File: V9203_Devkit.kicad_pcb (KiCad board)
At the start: 2 copper layers, 50 x 50 mm, 83 parts, among them J1 RJ45, J2 CONN_01X16, J3 CONN_01X12, J4 Screw_Terminal_1x04, J5 GROVE-CONNECTOR-SMD-90D(4+2P-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, J6 CONN_01X06, J7 GS3, J8 GS3, J9 CONN_01X06, U1 V9203, U2 ROF-78E, Y1 Crystal_GND24

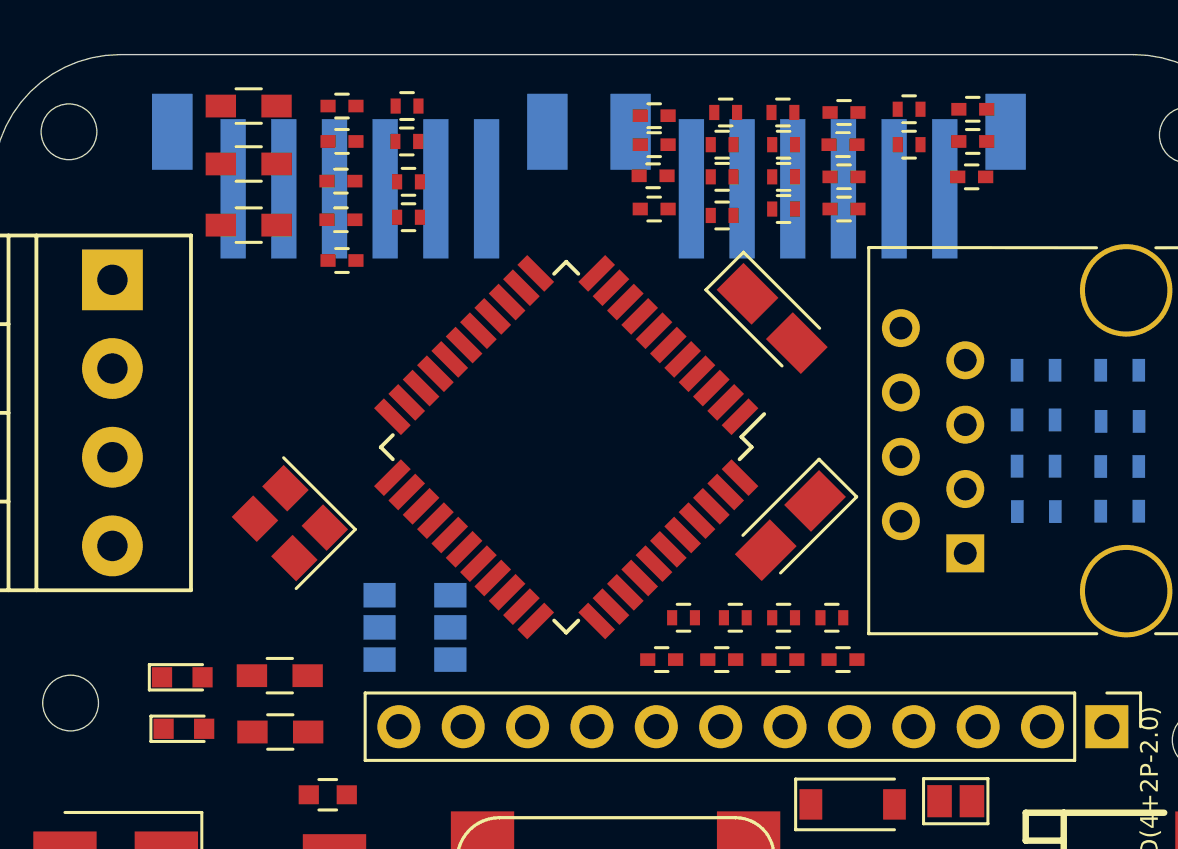
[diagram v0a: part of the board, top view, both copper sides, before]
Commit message: Added more signals to JST connector including DMA
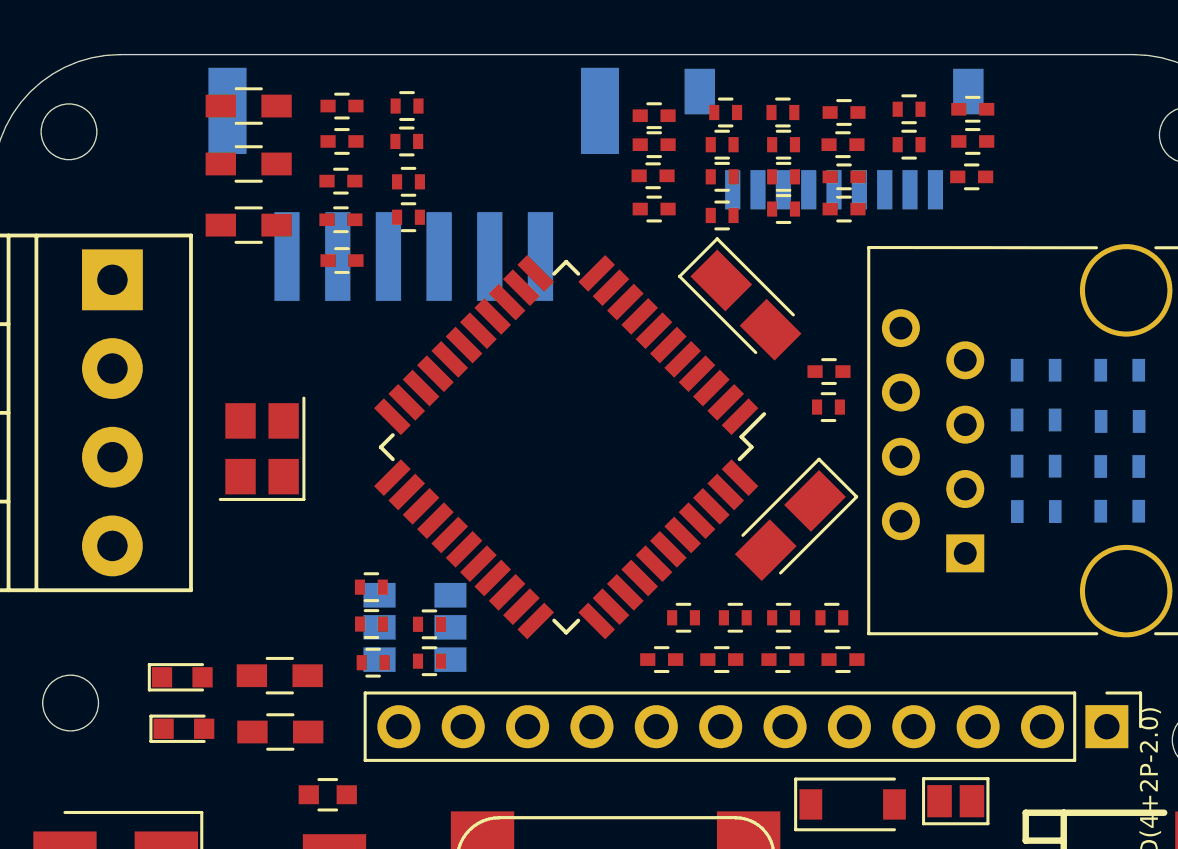
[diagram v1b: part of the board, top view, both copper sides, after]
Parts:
- added C27: C, Capacitors_SMD:C_0402, F.Cu at (143.0, 52.5)
- added R33: R, Resistors_SMD:R_0402, F.Cu at (143.0, 53.9)
- added R34: R, Resistors_SMD:R_0402, F.Cu at (124.9, 62.5)
- added R35: R, Resistors_SMD:R_0402, F.Cu at (124.9, 61.0)
- added R36: R, Resistors_SMD:R_0402, F.Cu at (127.2, 63.9)
- added R37: R, Resistors_SMD:R_0402, F.Cu at (125.0, 64.0)
- added R38: R, Resistors_SMD:R_0402, F.Cu at (127.2, 62.5)
- J6: value CONN_01X06 -> CONN_01X09; footprint Connectors_JST:JST_PH_B6B-PH-SM4-TB_06x2.00mm_Straight -> Connectors_JST:JST_SH_SM09B-SRSS-TB_09x1.00mm_Angled
- J9: footprint Connectors_JST:JST_PH_B6B-PH-SM4-TB_06x2.00mm_Straight -> Connectors_JST:JST_PH_S6B-PH-SM4-TB_06x2.00mm_Angled
- moved Y1 3.13 mm to (120.6, 55.6), turned to 90 degrees
- moved J9 2.32 mm to (126.6, 45.1), turned to 0 degrees
- moved C13 1.16 mm to (139.7, 49.9)
- moved J6 1.00 mm to (143.2, 43.4), turned to 0 degrees
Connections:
- C13 pad 2: Net-(C13-Pad2) -> +3V3
- C16 pad 1: Net-(C16-Pad1) -> +3V3
- J6 pad 6: GND -> Net-(J6-Pad6)
- U1 pad 2: Net-(C13-Pad2) -> +3V3
- U1 pad 30: Net-(J6-Pad5) -> Net-(R36-Pad1)
- U1 pad 31: Net-(J6-Pad4) -> Net-(R35-Pad1)
- U1 pad 32: Net-(J6-Pad3) -> Net-(R38-Pad1)
- U1 pad 33: Net-(J6-Pad2) -> Net-(R37-Pad1)
- U1 pad 34: Net-(J6-Pad1) -> Net-(R34-Pad1)
- U1 pad 35: Net-(U1-Pad35) -> Net-(J6-Pad3)
- U1 pad 36: Net-(U1-Pad36) -> Net-(J6-Pad2)
- U1 pad 37: Net-(U1-Pad37) -> Net-(J6-Pad1)
- U1 pad 44: Net-(C16-Pad1) -> +3V3

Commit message: Flipped connectors
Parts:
- C10, C11, C12, C15, C16, C17, C18, C19, C20, C21, C22, C5, C6, C7, C8, C9, R10, R11, R12, R13, R14, R15, R16, R2, R25, R26, R3, R4, R5, R6, R7, R8, R9: moved to B.Cu
- J6: moved to F.Cu
- J9: footprint Connectors_JST:JST_PH_S6B-PH-SM4-TB_06x2.00mm_Angled -> Connectors_JST:JST_SHL_SM06B-SHLS-TF_06x1.00mm_Angled; moved to F.Cu
- moved C22 13.4 mm to (149.4, 44.5), turned to 0 degrees
- moved C5 13.3 mm to (149.4, 43.3), turned to 180 degrees
- moved C6 13.3 mm to (149.4, 45.8), turned to 0 degrees
- moved C7 13.3 mm to (149.4, 42.2), turned to 180 degrees
- moved C10 11.8 mm to (136.8, 43.2), turned to 180 degrees
- moved C16 11.8 mm to (136.8, 41.9), turned to 180 degrees
- moved C15 11.8 mm to (136.9, 44.6), turned to 180 degrees
- moved R10 8.53 mm to (125.1, 49.0), turned to 270 degrees
- moved R2 7.95 mm to (146.7, 43.3), turned to 0 degrees
- moved R25 7.95 mm to (146.7, 44.6), turned to 0 degrees
- moved R26 7.95 mm to (146.7, 46.1), turned to 0 degrees
- moved R3 7.68 mm to (146.6, 42.0), turned to 180 degrees
- moved R16 6.84 mm to (120.7, 42.6), turned to 270 degrees
- moved R6 6.81 mm to (139.3, 41.9), turned to 180 degrees
- moved R7 6.81 mm to (139.3, 43.3), turned to 0 degrees
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
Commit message: Flipped connectors
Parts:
- moved LOGO1 4.58 mm to (134.8, 72.0)
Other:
- board text added: "V9203 3-phase low voltage Energy Monitor Featherwing http://whatnick.com"
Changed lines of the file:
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@@
     (area 107.306167 36.283 169.554549 91.950933)
     (thickness 1.6)
-    (drawings 10)
+    (drawings 11)
     (tracks 0)
     (zones 0)
@@
   )
   (module Symbols:OSHW-Logo2_7.3x6mm_SilkScreen (layer B.Cu)
-    (at 134.639429 76.574355 180)
+    (at 134.829929 72.002355 180)
     (descr "Open Source Hardware Symbol")
     (tags "Logo Symbol OSHW")
@@
     )
   )
+  (gr_text "V9203 3-phase low voltage\nEnergy Monitor Featherwing\nhttp://whatnick.com" (at 135.274429 80.828855) (layer B.SilkS)
+    (effects (font (size 1.5 1.5) (thickness 0.3)) (justify mirror))
+  )
   (gr_arc (start 115 85) (end 110 85) (angle -90) (layer Edge.Cuts) (width 0.01))

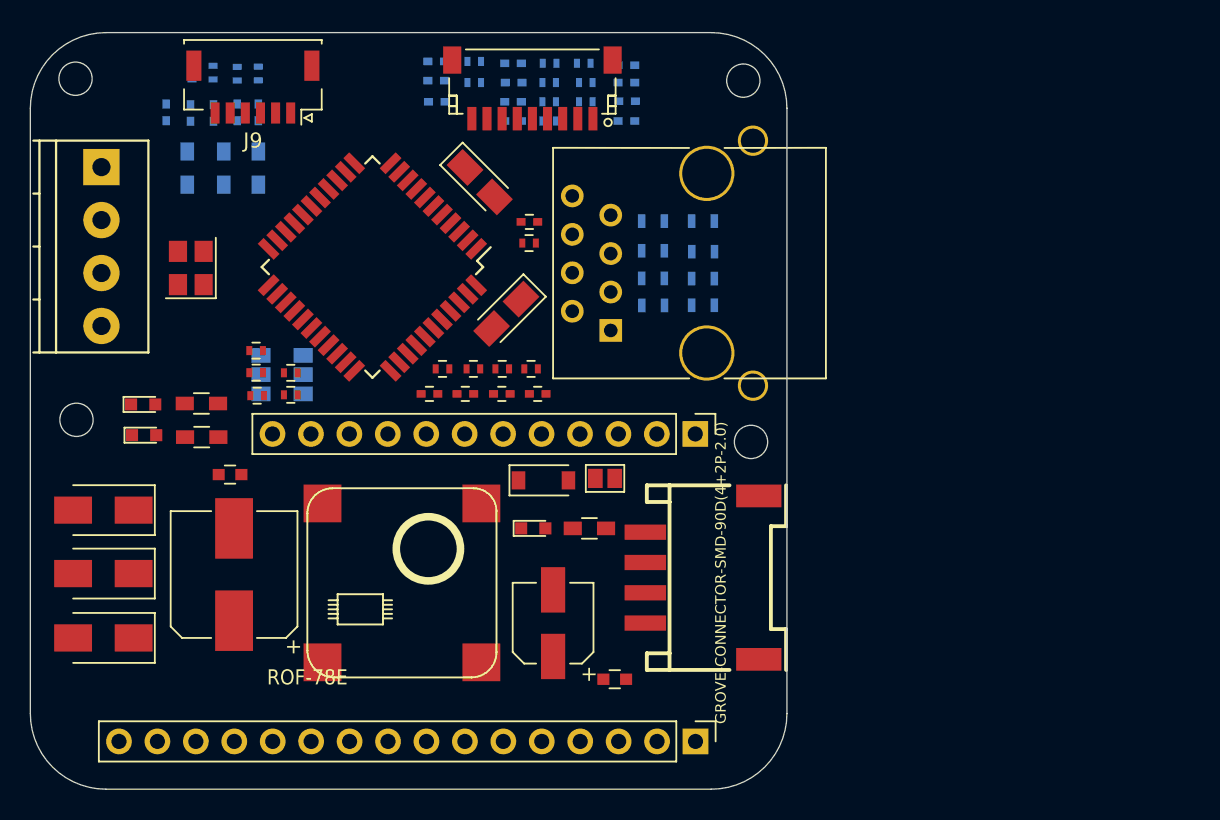
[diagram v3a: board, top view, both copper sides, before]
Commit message: Added PM0,1 and Deepsleep circuits
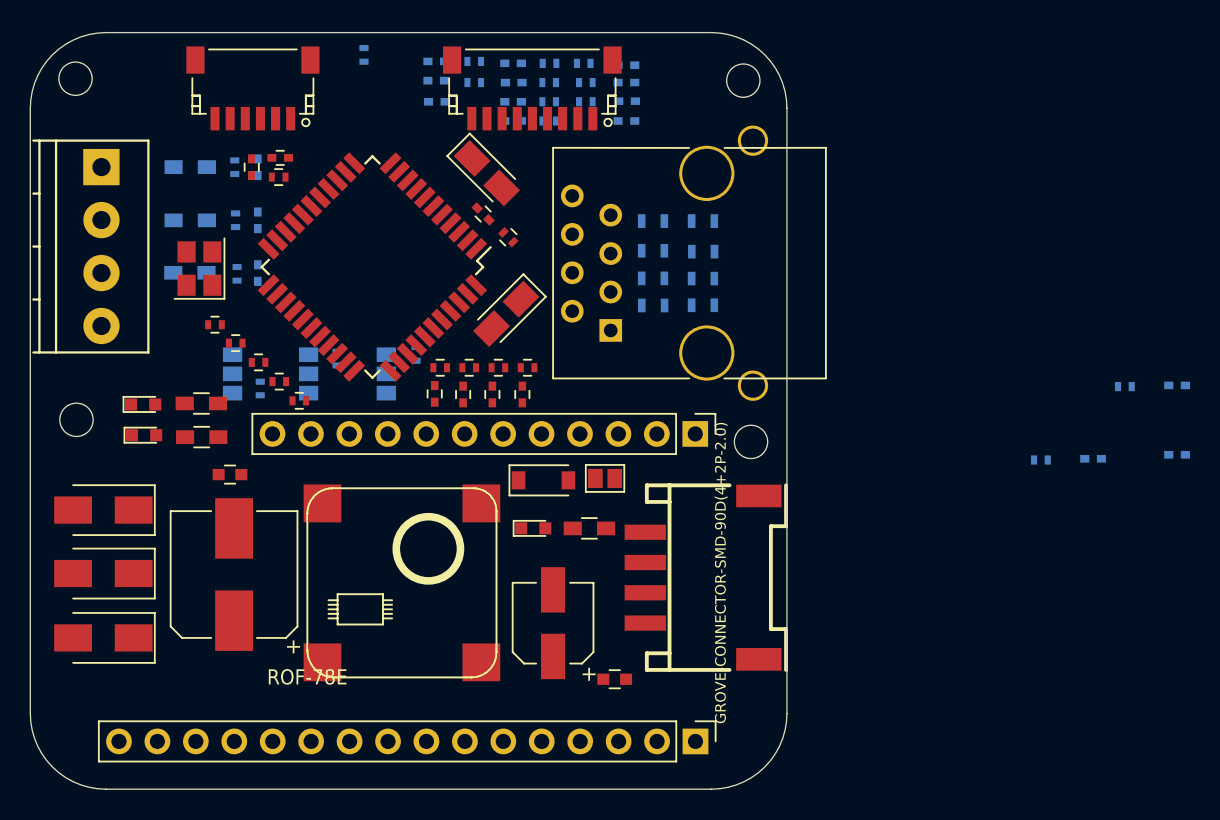
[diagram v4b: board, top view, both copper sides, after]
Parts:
- added C28: C, Capacitors_SMD:C_0402, B.Cu at (180.2, 68.2)
- added C29: C, Capacitors_SMD:C_0402, B.Cu at (185.8, 67.9)
- added C30: C, Capacitors_SMD:C_0402, B.Cu at (185.8, 63.3)
- added J10: GS3, Connect:GS3, B.Cu at (133.5, 62.6)
- added R39: R, Resistors_SMD:R_0402, B.Cu at (130.3, 61.5)
- added R40: R, Resistors_SMD:R_0402, B.Cu at (182.3, 63.4)
- added R41: R, Resistors_SMD:R_0402, B.Cu at (135.5, 61.2)
- added R42: R, Resistors_SMD:R_0402, B.Cu at (132.0, 41.5)
- added R43: R, Resistors_SMD:R_0402, B.Cu at (176.8, 68.2)
- added R44: R, Resistors_SMD:R_0402, B.Cu at (125.2, 63.5)
- C20, C21, R16: moved to F.Cu
- J9: footprint Connectors_JST:JST_SHL_SM06B-SHLS-TF_06x1.00mm_Angled -> Connectors_JST:JST_SH_SM06B-SRSS-TB_06x1.00mm_Angled
- moved R15 13.3 mm to (123.7, 55.9)
- moved C19 11.0 mm to (125.0, 55.9)
- moved R14 9.87 mm to (123.6, 52.4)
- moved R16 8.97 mm to (126.4, 49.5), turned to 180 degrees
- moved C18 7.26 mm to (125.0, 52.4)
- moved R12 6.92 mm to (120.5, 55.9), turned to 180 degrees
- moved R36 6.83 mm to (122.2, 59.3)
- moved C20 6.72 mm to (124.6, 48.9), turned to 270 degrees
- moved C21 6.63 mm to (126.5, 48.3), turned to 180 degrees
- moved R13 6.18 mm to (123.5, 48.9)
- moved R10 4.50 mm to (120.6, 48.9), turned to 180 degrees
- moved C23 4.16 mm to (140.5, 63.9), turned to 270 degrees
- moved R11 4.11 mm to (120.6, 52.4), turned to 180 degrees
- moved R31 4.10 mm to (137.1, 62.1)
- moved R32 4.09 mm to (139.0, 62.1)
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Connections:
- U1 pad 19: Net-(U1-Pad19) -> /V9203/DS
- U1 pad 21: Net-(U1-Pad21) -> +3V3
- U1 pad 24: Net-(J8-Pad2) -> Net-(C29-Pad1)
- U1 pad 25: Net-(J7-Pad2) -> Net-(C28-Pad1)

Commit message: Laid out components so far pending ERC,routing and review
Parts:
- added LOGO2: LOGO, Whatnick_logo:Whatnick_logo, B.Cu at (132.2, 53.3)
- C15, C16, C22, R25, R26: moved to F.Cu
- moved C29 58.1 mm to (128.3, 59.5), turned to 180 degrees
- moved C28 57.6 mm to (123.2, 59.5), turned to 180 degrees
- moved R40 57.2 mm to (125.2, 61.4), turned to 90 degrees
- moved C30 52.5 mm to (133.4, 59.5), turned to 180 degrees
- moved R43 41.6 mm to (135.4, 63.6), turned to 90 degrees
- moved C22 26.8 mm to (122.9, 48.3), turned to 180 degrees
- moved R25 24.5 mm to (122.8, 49.6)
- moved R26 22.6 mm to (124.6, 50.9)
- moved R42 22.3 mm to (130.3, 63.7)
- moved C16 19.3 mm to (142.8, 60.3), turned to 225 degrees
- moved C5 19.1 mm to (139.8, 59.8)
- moved R3 17.2 mm to (142.2, 58.6), turned to 0 degrees
- moved R2 17.1 mm to (142.2, 59.8)
- moved C15 16.0 mm to (138.9, 60.5), turned to 315 degrees
- moved C6 15.9 mm to (139.8, 58.6)
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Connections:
- C30 pad 2: +3V3 -> GND
- J10 pad 1: GND -> +3V3
- J10 pad 3: +3V3 -> GND
- R43 pad 1: GND -> +3V3

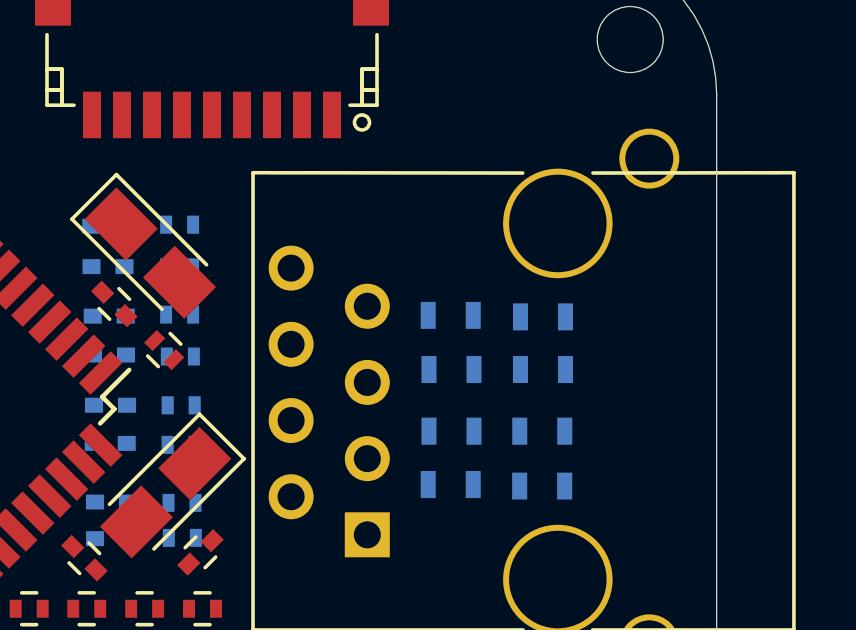
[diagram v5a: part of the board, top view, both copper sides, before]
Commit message: Ran ERC and updated pcb
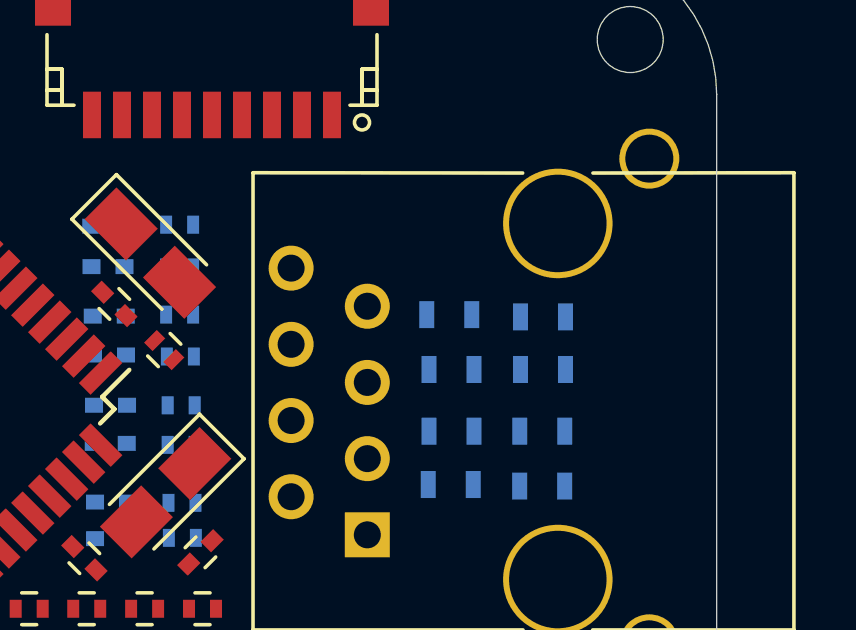
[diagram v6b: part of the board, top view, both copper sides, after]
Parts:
- moved R23 0.06 mm to (151.1, 52.3)
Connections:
- J1 pad 9: Net-(J1-Pad9) -> GND
- J4 pad 4: UN -> GND
- Y1 pad 2: Net-(Y1-Pad2) -> GND
- Y1 pad 4: Net-(Y1-Pad4) -> GND

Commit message: Set up for Freeroute
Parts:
- moved C15 8.21 mm to (140.5, 52.4), turned to 135 degrees
- moved R33 7.68 mm to (138.5, 60.6), turned to 315 degrees
- moved C27 2.44 mm to (138.2, 50.3)
- moved C13 0.53 mm to (140.8, 49.9)
- moved C14 0.31 mm to (141.4, 58.5)
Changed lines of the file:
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@@
   )
   (module Capacitors_SMD:C_0402 (layer F.Cu)
-    (at 139.922629 51.987155 315)
+    (at 138.16212 50.302846 315)
     (descr "Capacitor SMD 0402, reflow soldering, AVX (see smccp.pdf)")
     (tags "capacitor 0402")
@@
   )
   (module Resistors_SMD:R_0402 (layer F.Cu)
-    (at 141.585631 53.524553 135)
+    (at 138.512231 60.558957 315)
     (descr "Resistor SMD 0402, reflow soldering, Vishay (see dcrcw.pdf)")
     (tags "resistor 0402")
     (attr smd)
-    (fp_text reference R33 (at 0 -1.35 135) (layer F.SilkS)
-      (effects (font (size 0.001 0.001) (thickness 0.00025)))
-    )
-    (fp_text value R (at 0 1.45 135) (layer F.Fab)
+    (fp_text reference R33 (at 0 -1.35 315) (layer F.SilkS)
+      (effects (font (size 0.001 0.001) (thickness 0.00025)))
+    )
+    (fp_text value R (at 0 1.45 315) (layer F.Fab)
       (effects (font (size 1 1) (thickness 0.15)))
     )
@@
     (fp_line (start 0.5 0.25) (end -0.5 0.25) (layer F.Fab) (width 0.1))
     (fp_line (start -0.5 0.25) (end -0.5 -0.25) (layer F.Fab) (width 0.1))
-    (fp_text user %R (at 0 -1.35 135) (layer F.Fab)
-      (effects (font (size 1 1) (thickness 0.15)))
-    )
-    (pad 2 smd rect (at 0.45 0 135) (size 0.4 0.6) (layers F.Cu F.Paste F.Mask)
+    (fp_text user %R (at 0 -1.35 315) (layer F.Fab)
+      (effects (font (size 1 1) (thickness 0.15)))
+    )
+    (pad 2 smd rect (at 0.45 0 315) (size 0.4 0.6) (layers F.Cu F.Paste F.Mask)
       (net 53 +3V3))
-    (pad 1 smd rect (at -0.45 0 135) (size 0.4 0.6) (layers F.Cu F.Paste F.Mask)
+    (pad 1 smd rect (at -0.45 0 315) (size 0.4 0.6) (layers F.Cu F.Paste F.Mask)
       (net 86 "Net-(R33-Pad1)"))
     (model ${KISYS3DMOD}/Resistors_SMD.3dshapes/R_0402.wrl
@@
   )
   (module Capacitors_SMD:C_0402 (layer F.Cu)
-    (at 138.92412 60.462846 315)
+    (at 140.463938 52.401464 135)
     (descr "Capacitor SMD 0402, reflow soldering, AVX (see smccp.pdf)")
     (tags "capacitor 0402")
     (attr smd)
-    (fp_text reference C15 (at 0 -1.27 315) (layer F.SilkS)
-      (effects (font (size 0.001 0.001) (thickness 0.00025)))
-    )
-    (fp_text value C (at 0 1.27 315) (layer F.Fab)
+    (fp_text reference C15 (at 0 -1.27 135) (layer F.SilkS)
+      (effects (font (size 0.001 0.001) (thickness 0.00025)))
+    )
+    (fp_text value C (at 0 1.27 135) (layer F.Fab)
       (effects (font (size 1 1) (thickness 0.15)))
     )
@@
     (fp_line (start 0.5 0.25) (end -0.5 0.25) (layer F.Fab) (width 0.1))
     (fp_line (start -0.5 0.25) (end -0.5 -0.25) (layer F.Fab) (width 0.1))
-    (fp_text user %R (at 0 -1.27 315) (layer F.Fab)
-      (effects (font (size 1 1) (thickness 0.15)))
-    )
-    (pad 2 smd rect (at 0.55 0 315) (size 0.6 0.5) (layers F.Cu F.Paste F.Mask)
+    (fp_text user %R (at 0 -1.27 135) (layer F.Fab)
+      (effects (font (size 1 1) (thickness 0.15)))
+    )
+    (pad 2 smd rect (at 0.55 0 135) (size 0.6 0.5) (layers F.Cu F.Paste F.Mask)
       (net 33 "Net-(C14-Pad2)"))
-    (pad 1 smd rect (at -0.55 0 315) (size 0.6 0.5) (layers F.Cu F.Paste F.Mask)
+    (pad 1 smd rect (at -0.55 0 135) (size 0.6 0.5) (layers F.Cu F.Paste F.Mask)
       (net 35 "Net-(C13-Pad1)"))
     (model Capacitors_SMD.3dshapes/C_0402.wrl
@@
   )
   (module Capacitors_Tantalum_SMD:CP_Tantalum_Case-A_EIA-3216-18_Reflow (layer F.Cu)
-    (at 141.631501 58.279283 225)
+    (at 141.388757 58.471227 225)
     (descr "Tantalum capacitor, Case A, EIA 3216-18, 3.2x1.6x1.6mm, Reflow soldering footprint")
     (tags "capacitor tantalum smd")
@@
   )
   (module Capacitors_Tantalum_SMD:CP_Tantalum_Case-A_EIA-3216-18_Reflow (layer F.Cu)
-    (at 141.123501 50.292427 315)
+    (at 140.818701 49.860627 315)
     (descr "Tantalum capacitor, Case A, EIA 3216-18, 3.2x1.6x1.6mm, Reflow soldering footprint")
     (tags "capacitor tantalum smd")

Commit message: Freeroute run
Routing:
- net GND: track 0.00 -> 339.4 mm, vias 0 -> 4
- net +3V3: track 0.00 -> 207.8 mm, vias 0 -> 6
- net MISO: track 0.00 -> 109.5 mm, vias 0 -> 3
- net MOSI: track 0.00 -> 98.0 mm, vias 0 -> 3
- net SCK: track 0.00 -> 82.2 mm, vias 0 -> 3
- net Net-(J6-Pad4): track 0.00 -> 69.7 mm, vias 0 -> 2
- net Net-(J6-Pad6): track 0.00 -> 51.7 mm
- net Net-(J6-Pad5): track 0.00 -> 50.1 mm, vias 0 -> 2
- net Net-(J6-Pad7): track 0.00 -> 44.1 mm
- net Net-(J6-Pad8): track 0.00 -> 39.7 mm
- net UB: track 0.00 -> 36.1 mm
- net CS: track 0.00 -> 35.8 mm, vias 0 -> 2
- net Net-(J6-Pad3): track 0.00 -> 33.9 mm, vias 0 -> 2
- net UA: track 0.00 -> 33.9 mm
- net Net-(C1-Pad1): track 0.00 -> 32.3 mm
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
